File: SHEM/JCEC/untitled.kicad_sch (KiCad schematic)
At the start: 31 parts, among them U1 TL082, U2 TL082, U3 TL082

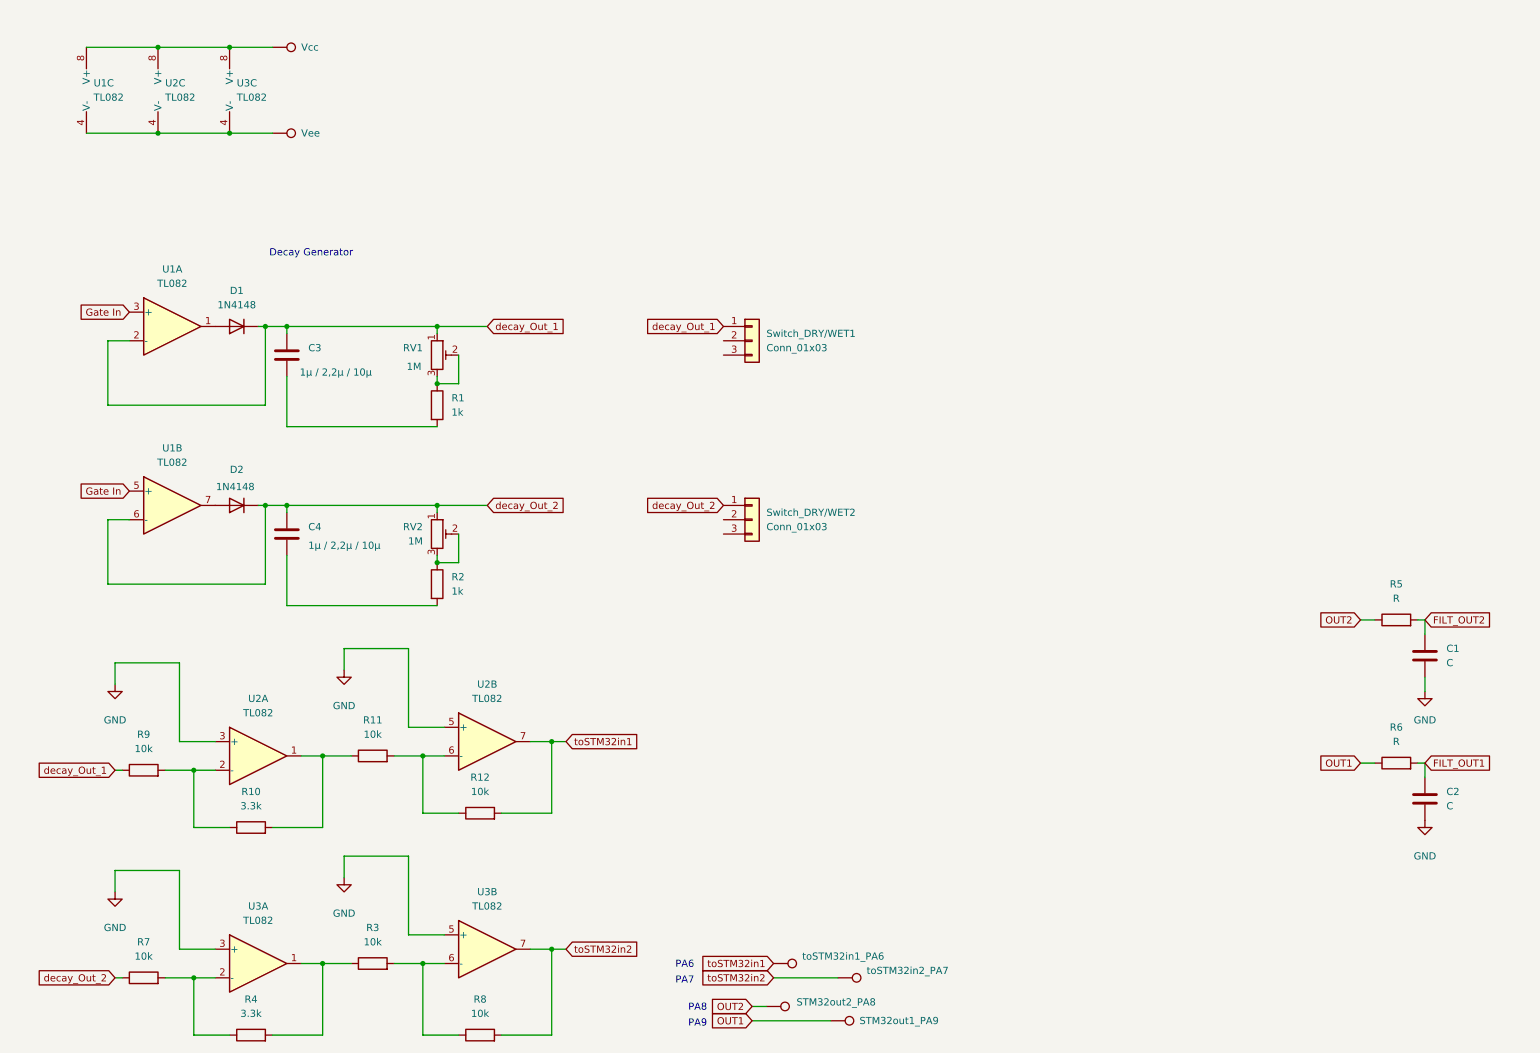
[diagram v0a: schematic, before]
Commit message: Quantizer + début boite noire
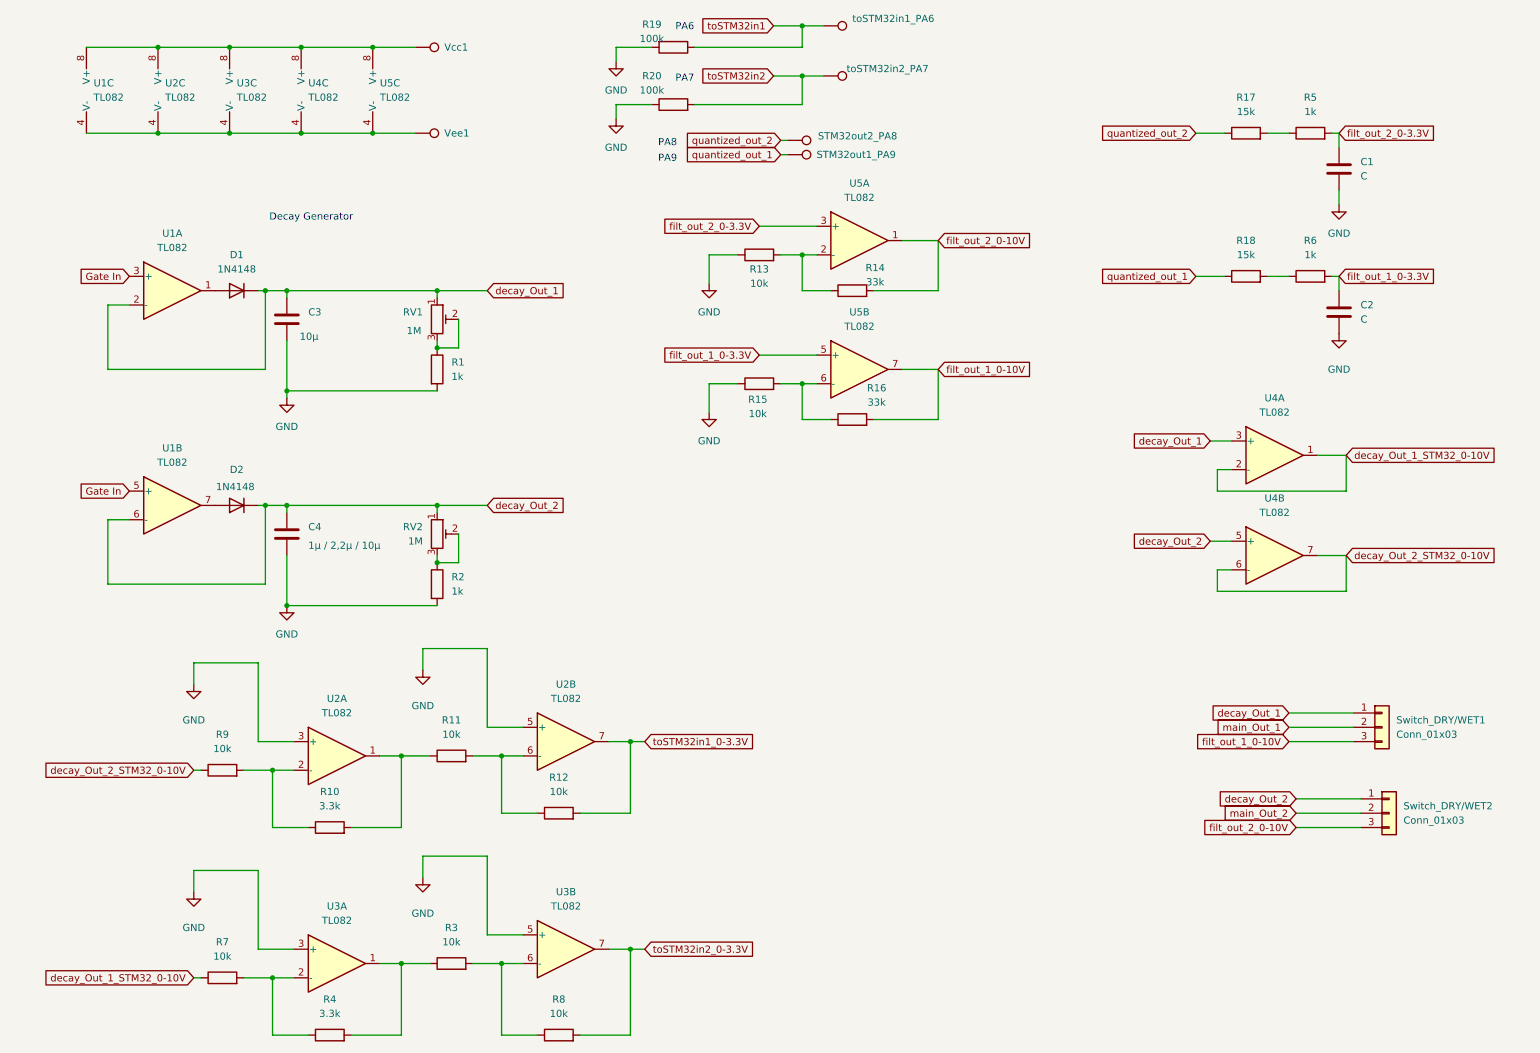
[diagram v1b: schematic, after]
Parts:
- added R13, R15: 10k, Resistor_THT:R_Axial_DIN0204_L3.6mm_D1.6mm_P5.08mm_Horizontal, symbol Device:R
- added R14, R16: 33k, Resistor_THT:R_Axial_DIN0204_L3.6mm_D1.6mm_P5.08mm_Horizontal, symbol Device:R
- added R17, R18: 15k, Resistor_THT:R_Axial_DIN0204_L3.6mm_D1.6mm_P5.08mm_Horizontal, symbol Device:R
- added R19, R20: 100k, Resistor_THT:R_Axial_DIN0204_L3.6mm_D1.6mm_P5.08mm_Horizontal, symbol Device:R
- added U4, U5: TL082, Package_DIP:DIP-8_W7.62mm_LongPads, symbol Amplifier_Operational:TL082
- C3: value 1µ / 2,2µ / 10µ -> 10µ
- R5, R6: value R -> 1k
- U1: footprint Package_DIP:DIP-8_W7.62mm -> Package_DIP:DIP-8_W7.62mm_LongPads
- U2, U3: footprint (none) -> Package_DIP:DIP-8_W7.62mm_LongPads
- renumbered Vcc to Vcc1, Vee to Vee1
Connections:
- net GND: now also C3.2, C4.2, R1.2, R2.2, R13.1, R15.1, R19.2, R20.1
- net decay_Out_1: now also U4.3 (+); no longer R9.1
- net decay_Out_2: now also U4.5 (+); no longer R7.1
- net toSTM32in1: now also R19.1; no longer R12.2, U2.7
- net toSTM32in2: now also R20.2; no longer R8.2, U3.7
- net main_Out_1: now reaches Switch_DRY/WET1.2 (Pin_2)
- net filt_out_1_0-10V: now reaches Switch_DRY/WET1.3 (Pin_3)
- net filt_out_1_0-10V: now also R16.2, U5.7
- net at U1.4 (V-), U2.4 (V-), U3.4 (V-)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: now also U4.4 (V-), U5.4 (V-)
- net at U1.8 (V+), U2.8 (V+), U3.8 (V+)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: now also U4.8 (V+), U5.8 (V+)
- net main_Out_2: now reaches Switch_DRY/WET2.2 (Pin_2)
- net filt_out_2_0-10V: now reaches Switch_DRY/WET2.3 (Pin_3)
- net filt_out_2_0-10V: now also R14.2, U5.1
- net FILT_OUT1 renamed filt_out_1_0-3.3V
- net filt_out_1_0-3.3V: now also U5.5 (+)
- net FILT_OUT2 renamed filt_out_2_0-3.3V
- net filt_out_2_0-3.3V: now also U5.3 (+)
- net OUT1: no longer names the net of R6.1
- net OUT1: now also R18.2; no longer STM32out1_PA9.1
- net OUT2: no longer names the net of R5.1
- net OUT2: now also R17.2; no longer STM32out2_PA8.1
- new net: R15.2, R16.1, U5.6 (-)
- new net: R13.2, R14.1, U5.2 (-)
- new net decay_Out_1_STM32_0-10V: R7.1, U4.1, U4.2 (-)
- new net decay_Out_2_STM32_0-10V: R9.1, U4.6 (-), U4.7
- new net quantized_out_1: R18.1, STM32out1_PA9.1
- new net quantized_out_2: R17.1, STM32out2_PA8.1
- new net toSTM32in1_0-3.3V: R12.2, U2.7
- new net toSTM32in2_0-3.3V: R8.2, U3.7
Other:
- moved on the sheet: C1, C2, C3, D1, R1, R10, R11, R12, R3, R4, R5, R6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

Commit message: Update
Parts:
- added GND1, main_Out_1, main_Out_2: TestPoint, Connector_Pin:Pin_D1.0mm_L10.0mm, symbol Connector:TestPoint
- R1, R10, R13, R14, R15, R16, R17, R18, R19, R2, R20, R3, R4, R5, R6, R7, R8, R9: footprint Resistor_THT:R_Axial_DIN0204_L3.6mm_D1.6mm_P5.08mm_Horizontal -> Resistor_THT:R_Axial_DIN0207_L6.3mm_D2.5mm_P10.16mm_Horizontal
- R11, R12: footprint Resistor_THT:R_Axial_DIN0204_L3.6mm_D1.6mm_P7.62mm_Horizontal -> Resistor_THT:R_Axial_DIN0207_L6.3mm_D2.5mm_P10.16mm_Horizontal
- RV1, RV2: footprint Resistor_THT:R_Axial_DIN0204_L3.6mm_D1.6mm_P1.90mm_Vertical -> Resistor_THT:R_Axial_DIN0207_L6.3mm_D2.5mm_P10.16mm_Horizontal
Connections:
- net GND: now also GND1.1
- net main_Out_1: now also main_Out_1.1
- net main_Out_2: now also main_Out_2.1
